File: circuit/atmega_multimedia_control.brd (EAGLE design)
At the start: 98.7 x 81.3 mm, 12 parts, among them IC1 MEGA8-P, Q1 20Mhz

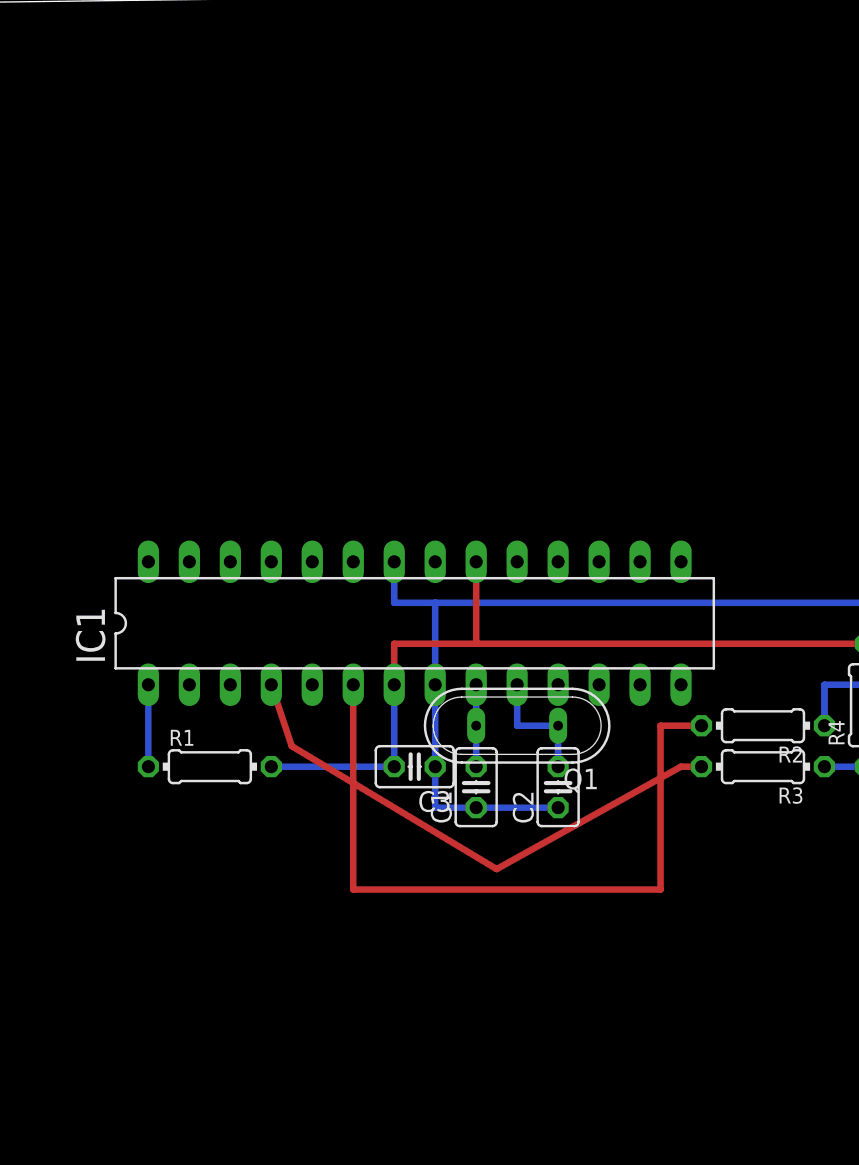
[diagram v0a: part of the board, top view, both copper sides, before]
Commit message: circuit and board done
volume knob is missing from board. some led resistors still need proper
placement, will sort that out during soldering
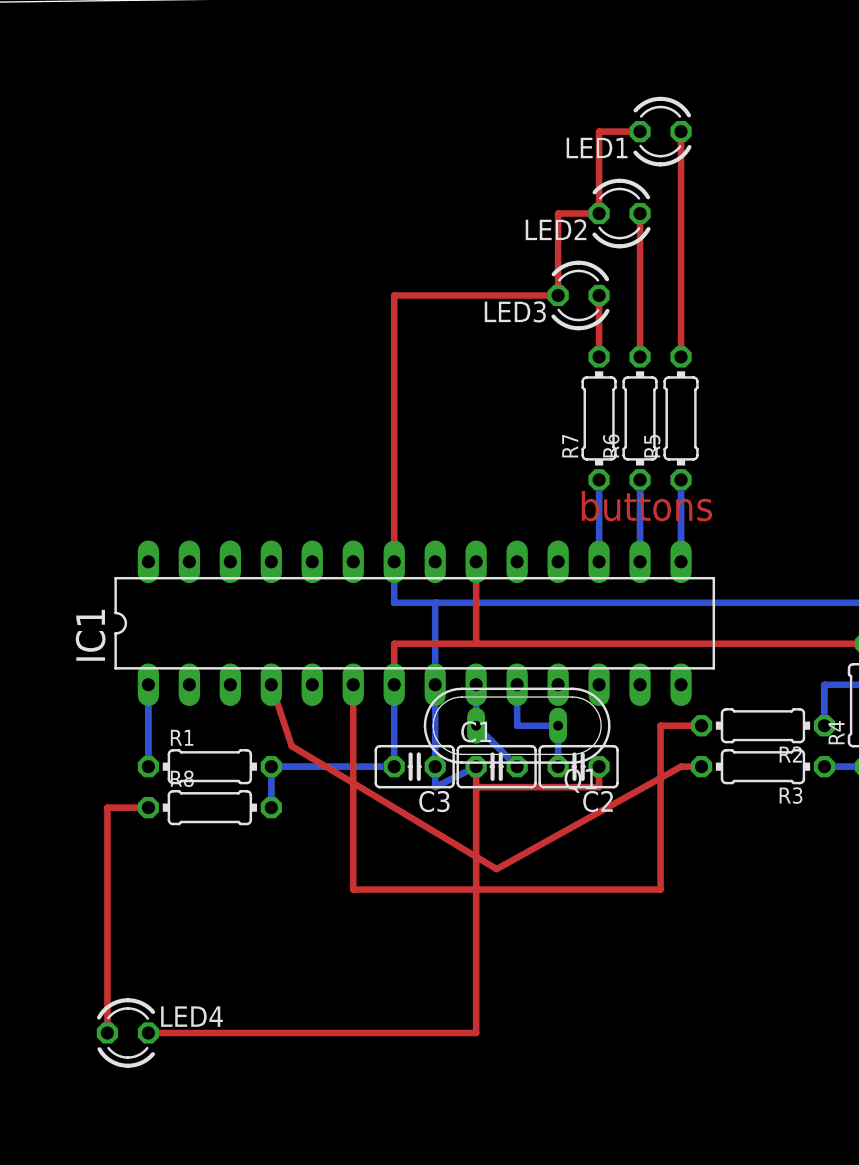
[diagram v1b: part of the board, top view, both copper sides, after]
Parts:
- added LED1, LED2, LED3, LED4: (no value), led:LED3MM
- added R5, R6, R7, R8: 2k2, rcl:0204/7
- X1: value (none) -> USB
- moved C1 1.80 mm to (63.5, 33.0), turned to 0 degrees
- moved C2 1.80 mm to (68.6, 33.0), turned to 180 degrees
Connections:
- removed net +5V: C3.2, IC1.20, IC1.7, R1.2, R4.2, X1.1
- new net N$10: LED1.A, R5.2
- new net N$11: IC1.16, R6.1
- new net N$12: LED2.A, R6.2
- new net N$13: IC1.17, R7.1
- new net N$14: LED3.A, R7.2
- new net N$15: LED4.A, R8.1
- new net N$9: IC1.15, R5.1
- new net VCC: C3.2, IC1.20, IC1.7, R1.2, R4.2, R8.2, X1.1
- net GND: now also LED1.K, LED2.K, LED3.K, LED4.K
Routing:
- net GND: track 70.0 -> 151.6 mm
- net VCC: track 0.00 -> 60.1 mm
- net +5V: track 57.5 -> 0.00 mm
- net N$15: track 0.00 -> 16.5 mm
- net N$10: track 0.00 -> 14.0 mm
- net N$12: track 0.00 -> 8.89 mm
- net N$9: track 0.00 -> 5.08 mm
- net N$13: track 0.00 -> 5.08 mm
- net N$11: track 0.00 -> 5.08 mm
- net N$14: track 0.00 -> 3.81 mm
- net N$2: track 5.08 -> 6.13 mm
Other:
- board text added: "buttons"
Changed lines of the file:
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@@
 <wire x1="98.73" y1="81.27" x2="0" y2="80" width="0" layer="20"/>
 <wire x1="0" y1="80" x2="0" y2="0" width="0" layer="20"/>
+<text x="68.58" y="48.26" size="1.778" layer="1">buttons</text>
 </plain>
 <attributes>
@@
 <attribute name="OC_FARNELL" value="unknown" x="90.17" y="16.51" size="1.778" layer="27" display="off"/>
 </element>
-<element name="C1" library="rcl" package="C025-025X050" value="22p" x="62.23" y="31.75" rot="R90"/>
+<element name="C1" library="rcl" package="C025-025X050" value="22p" x="63.5" y="33.02"/>
 <element name="R1" library="rcl" package="0204/7" value="100k" x="45.72" y="33.02"/>
-<element name="C2" library="rcl" package="C025-025X050" value="22p" x="67.31" y="31.75" rot="R90"/>
-<element name="X1" library="con-berg" package="PN61729" value="" x="99.06" y="39.37" rot="R90">
+<element name="C2" library="rcl" package="C025-025X050" value="22p" x="68.58" y="33.02" rot="R180"/>
+<element name="X1" library="con-berg" package="PN61729" value="USB" x="99.06" y="39.37" rot="R90">
 <attribute name="OC_NEWARK" value="unknown" x="110.49" y="59.69" size="1.778" layer="27" rot="R90" display="off"/>
 <attribute name="MPN" value="" x="110.49" y="59.69" size="1.778" layer="27" rot="R90" display="off"/>
@@
 <element name="R4" library="rcl" package="0204/7" value="2k2" x="86.36" y="36.83" rot="R90"/>
 <element name="C3" library="rcl" package="C025-025X050" value="100n" x="58.42" y="33.02" rot="R180"/>
+<element name="LED1" library="led" package="LED3MM" value="" x="73.66" y="72.39" rot="R180"/>
+<element name="LED2" library="led" package="LED3MM" value="" x="71.12" y="67.31" rot="R180"/>
+<element name="LED3" library="led" package="LED3MM" value="" x="68.58" y="62.23" rot="R180"/>
+<element name="R5" library="rcl" package="0204/7" value="2k2" x="74.93" y="54.61" rot="R90"/>
+<element name="R6" library="rcl" package="0204/7" value="2k2" x="72.39" y="54.61" rot="R90"/>
+<element name="R7" library="rcl" package="0204/7" value="2k2" x="69.85" y="54.61" rot="R90"/>
+<element name="LED4" library="led" package="LED3MM" value="" x="40.64" y="16.51"/>
+<element name="R8" library="rcl" package="0204/7" value="2k2" x="45.72" y="30.48"/>
 </elements>
 <signals>
-<signal name="+5V">
-<contactref element="R1" pad="2"/>
-<contactref element="IC1" pad="20"/>
-<contactref element="X1" pad="1"/>
-<contactref element="R4" pad="2"/>
-<contactref element="C3" pad="2"/>
-<wire x1="57.15" y1="40.64" x2="62.23" y2="40.64" width="0.4064" layer="1"/>
-<wire x1="62.23" y1="40.64" x2="62.23" y2="45.72" width="0.4064" layer="1"/>
-<wire x1="94.35" y1="40.62" x2="86.36" y2="40.62" width="0.4064" layer="16"/>
-<wire x1="86.36" y1="40.62" x2="86.36" y2="40.64" width="0.4064" layer="16"/>
-<contactref element="IC1" pad="7"/>
-<wire x1="49.53" y1="33.02" x2="57.15" y2="33.02" width="0.4064" layer="16"/>
-<wire x1="57.15" y1="33.02" x2="57.15" y2="38.1" width="0.4064" layer="16"/>
-<wire x1="57.15" y1="38.1" x2="57.15" y2="40.64" width="0.4064" layer="1"/>
-<wire x1="62.23" y1="40.64" x2="86.36" y2="40.64" width="0.4064" layer="1"/>
-</signal>
 <signal name="N$1">
 <contactref element="R1" pad="1"/>
@@
 <contactref element="C1" pad="1"/>
 <contactref element="C2" pad="1"/>
-<wire x1="59.69" y1="33.02" x2="59.69" y2="30.48" width="0.4064" layer="16"/>
-<wire x1="59.69" y1="30.48" x2="62.23" y2="30.48" width="0.4064" layer="16"/>
-<wire x1="62.23" y1="30.48" x2="67.31" y2="30.48" width="0.4064" layer="16"/>
+<wire x1="59.69" y1="33.02" x2="59.69" y2="31.75" width="0.4064" layer="16"/>
+<wire x1="59.69" y1="31.75" x2="62.23" y2="33.02" width="0.4064" layer="16"/>
+<contactref element="LED1" pad="K"/>
+<contactref element="LED2" pad="K"/>
+<contactref element="LED3" pad="K"/>
+<contactref element="LED4" pad="K"/>
+<wire x1="67.31" y1="62.23" x2="57.15" y2="62.23" width="0.4064" layer="1"/>
+<wire x1="57.15" y1="62.23" x2="57.15" y2="45.72" width="0.4064" layer="1"/>
+<wire x1="67.31" y1="62.23" x2="67.31" y2="67.31" width="0.4064" layer="1"/>
+<wire x1="67.31" y1="67.31" x2="69.85" y2="67.31" width="0.4064" layer="1"/>
+<wire x1="69.85" y1="67.31" x2="69.85" y2="72.39" width="0.4064" layer="1"/>
+<wire x1="69.85" y1="72.39" x2="72.39" y2="72.39" width="0.4064" layer="1"/>
+<wire x1="41.91" y1="16.51" x2="62.23" y2="16.51" width="0.4064" layer="1"/>
+<wire x1="62.23" y1="16.51" x2="62.23" y2="31.75" width="0.4064" layer="1"/>
+<wire x1="62.23" y1="33.02" x2="62.23" y2="31.75" width="0.4064" layer="1"/>
+<wire x1="62.23" y1="31.75" x2="69.85" y2="31.75" width="0.4064" layer="1"/>
+<wire x1="69.85" y1="31.75" x2="69.85" y2="33.02" width="0.4064" layer="1"/>
 </signal>
 <signal name="N$6">
@@
 <contactref element="IC1" pad="9"/>
 <wire x1="62.23" y1="38.1" x2="62.23" y2="35.56" width="0.4064" layer="16"/>
-<wire x1="62.23" y1="35.56" x2="62.23" y2="33.02" width="0.4064" layer="16"/>
+<wire x1="62.23" y1="35.56" x2="64.77" y2="33.02" width="0.4064" layer="16"/>
 </signal>
 <signal name="N$3">
@@
 <wire x1="64.77" y1="35.56" x2="64.77" y2="38.1" width="0.4064" layer="16"/>
 </signal>
+<signal name="N$9">
+<contactref element="IC1" pad="15"/>
+<contactref element="R5" pad="1"/>
+<wire x1="74.93" y1="50.8" x2="74.93" y2="45.72" width="0.4064" layer="16"/>
+</signal>
+<signal name="N$10">
+<contactref element="R5" pad="2"/>
+<contactref element="LED1" pad="A"/>
+<wire x1="74.93" y1="58.42" x2="74.93" y2="72.39" width="0.4064" layer="1"/>
+</signal>
+<signal name="N$11">
+<contactref element="IC1" pad="16"/>
+<contactref element="R6" pad="1"/>
+<wire x1="72.39" y1="50.8" x2="72.39" y2="45.72" width="0.4064" layer="16"/>
+</signal>
+<signal name="N$12">
+<contactref element="R6" pad="2"/>
+<contactref element="LED2" pad="A"/>
+<wire x1="72.39" y1="58.42" x2="72.39" y2="67.31" width="0.4064" layer="1"/>
+</signal>
+<signal name="N$13">
+<contactref element="IC1" pad="17"/>
+<contactref element="R7" pad="1"/>
+<wire x1="69.85" y1="50.8" x2="69.85" y2="45.72" width="0.4064" layer="16"/>
+</signal>
+<signal name="N$14">
+<contactref element="R7" pad="2"/>
+<contactref element="LED3" pad="A"/>
+<wire x1="69.85" y1="58.42" x2="69.85" y2="62.23" width="0.4064" layer="1"/>
+</signal>
+<signal name="N$15">
+<contactref element="LED4" pad="A"/>
+<contactref element="R8" pad="1"/>
+<wire x1="41.91" y1="30.48" x2="39.37" y2="30.48" width="0.4064" layer="1"/>
+<wire x1="39.37" y1="30.48" x2="39.37" y2="16.51" width="0.4064" layer="1"/>
+</signal>
+<signal name="VCC">
+<contactref element="R1" pad="2"/>
+<contactref element="IC1" pad="20"/>
+<contactref element="X1" pad="1"/>
+<contactref element="R4" pad="2"/>
+<contactref element="C3" pad="2"/>
+<contactref element="IC1" pad="7"/>
+<contactref element="R8" pad="2"/>
+<wire x1="57.15" y1="40.64" x2="62.23" y2="40.64" width="0.4064" layer="1"/>
+<wire x1="62.23" y1="40.64" x2="62.23" y2="45.72" width="0.4064" layer="1"/>
+<wire x1="94.35" y1="40.62" x2="86.36" y2="40.62" width="0.4064" layer="16"/>
+<wire x1="86.36" y1="40.62" x2="86.36" y2="40.64" width="0.4064" layer="16"/>
+<wire x1="49.53" y1="33.02" x2="57.15" y2="33.02" width="0.4064" layer="16"/>
+<wire x1="57.15" y1="33.02" x2="57.15" y2="38.1" width="0.4064" layer="16"/>
+<wire x1="57.15" y1="38.1" x2="57.15" y2="40.64" width="0.4064" layer="1"/>
+<wire x1="62.23" y1="40.64" x2="86.36" y2="40.64" width="0.4064" layer="1"/>
+<wire x1="49.53" y1="33.02" x2="49.53" y2="30.48" width="0.4064" layer="16"/>
+</signal>
 </signals>

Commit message: fixed schematic
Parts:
- moved R2 2.54 mm to (80.0, 33.0)
- moved R3 2.54 mm to (80.0, 35.6)
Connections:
- removed net N$5 (its old number): D2.C, R3.1, R4.1, X1.3
- removed net N$6: D1.C, R2.1, X1.2
- new net N$16: D1.C, R2.1, R4.1, X1.2
- new net N$4: D2.C, R3.1, X1.3
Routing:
- net N$16: track 0.00 -> 18.2 mm
- net N$5 (its old number): track 18.0 -> 0.00 mm
- net N$4: track 0.00 -> 15.4 mm
- net N$7: track 33.2 -> 47.0 mm
- net N$6: track 13.1 -> 0.00 mm
- net N$5: track 44.5 -> 34.3 mm
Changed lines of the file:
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@@
 <element name="D1" library="diode" package="DO34Z7" value="3v6" x="91.44" y="41.91" rot="R90"/>
 <element name="D2" library="diode" package="DO34Z7" value="3v6" x="88.9" y="39.37" rot="R90"/>
-<element name="R2" library="rcl" package="0204/7" value="68" x="80.01" y="35.56" rot="R180"/>
-<element name="R3" library="rcl" package="0204/7" value="68" x="80.01" y="33.02" rot="R180"/>
+<element name="R2" library="rcl" package="0204/7" value="68" x="80.01" y="33.02" rot="R180"/>
+<element name="R3" library="rcl" package="0204/7" value="68" x="80.01" y="35.56" rot="R180"/>
 <element name="Q1" library="special" package="QS" value="20Mhz" x="64.77" y="35.56" rot="R180"/>
 <element name="R4" library="rcl" package="0204/7" value="2k2" x="86.36" y="36.83" rot="R90"/>
@@
 <wire x1="62.23" y1="31.75" x2="69.85" y2="31.75" width="0.4064" layer="1"/>
 <wire x1="69.85" y1="31.75" x2="69.85" y2="33.02" width="0.4064" layer="1"/>
-</signal>
-<signal name="N$6">
-<contactref element="X1" pad="2"/>
-<contactref element="R2" pad="1"/>
-<contactref element="D1" pad="C"/>
-<wire x1="91.44" y1="38.1" x2="94.35" y2="38.1" width="0.4064" layer="16"/>
-<wire x1="94.35" y1="38.1" x2="94.35" y2="38.12" width="0.4064" layer="16"/>
-<wire x1="83.82" y1="35.56" x2="83.82" y2="38.1" width="0.4064" layer="16"/>
-<wire x1="83.82" y1="38.1" x2="91.44" y2="38.1" width="0.4064" layer="16"/>
-</signal>
-<signal name="N$4">
-<contactref element="R2" pad="2"/>
-<contactref element="IC1" pad="6"/>
-<wire x1="76.2" y1="35.56" x2="73.66" y2="35.56" width="0.4064" layer="1"/>
-<wire x1="73.66" y1="35.56" x2="73.66" y2="25.4" width="0.4064" layer="1"/>
-<wire x1="73.66" y1="25.4" x2="54.61" y2="25.4" width="0.4064" layer="1"/>
-<wire x1="54.61" y1="25.4" x2="54.61" y2="38.1" width="0.4064" layer="1"/>
-</signal>
-<signal name="N$5">
-<contactref element="R3" pad="1"/>
-<contactref element="X1" pad="3"/>
-<contactref element="R4" pad="1"/>
-<contactref element="D2" pad="C"/>
-<wire x1="96.35" y1="38.12" x2="96.52" y2="38.12" width="0.4064" layer="16"/>
-<wire x1="96.52" y1="38.12" x2="96.52" y2="35.56" width="0.4064" layer="16"/>
-<wire x1="96.52" y1="35.56" x2="88.9" y2="35.56" width="0.4064" layer="16"/>
-<wire x1="88.9" y1="35.56" x2="88.9" y2="33.02" width="0.4064" layer="16"/>
-<wire x1="88.9" y1="33.02" x2="86.36" y2="33.02" width="0.4064" layer="16"/>
-<wire x1="83.82" y1="33.02" x2="86.36" y2="33.02" width="0.4064" layer="16"/>
-</signal>
-<signal name="N$7">
-<contactref element="R3" pad="2"/>
-<contactref element="IC1" pad="4"/>
-<wire x1="49.53" y1="38.1" x2="50.8" y2="34.29" width="0.4064" layer="1"/>
-<wire x1="50.8" y1="34.29" x2="63.5" y2="26.67" width="0.4064" layer="1"/>
-<wire x1="63.5" y1="26.67" x2="74.93" y2="33.02" width="0.4064" layer="1"/>
-<wire x1="74.93" y1="33.02" x2="76.2" y2="33.02" width="0.4064" layer="1"/>
 </signal>
 <signal name="N$8">
@@
 <wire x1="49.53" y1="33.02" x2="49.53" y2="30.48" width="0.4064" layer="16"/>
 </signal>
+<signal name="N$4">
+<contactref element="X1" pad="3"/>
+<contactref element="D2" pad="C"/>
+<wire x1="96.35" y1="38.12" x2="96.52" y2="38.12" width="0.4064" layer="16"/>
+<wire x1="96.52" y1="38.12" x2="96.52" y2="35.56" width="0.4064" layer="16"/>
+<wire x1="96.52" y1="35.56" x2="88.9" y2="35.56" width="0.4064" layer="16"/>
+<contactref element="R3" pad="1"/>
+<wire x1="83.82" y1="35.56" x2="88.9" y2="35.56" width="0.4064" layer="1"/>
+</signal>
+<signal name="N$5">
+<contactref element="R2" pad="2"/>
+<contactref element="IC1" pad="6"/>
+<wire x1="76.2" y1="33.02" x2="76.2" y2="29.21" width="0.4064" layer="1"/>
+<wire x1="76.2" y1="29.21" x2="54.61" y2="29.21" width="0.4064" layer="1"/>
+<wire x1="54.61" y1="29.21" x2="54.61" y2="38.1" width="0.4064" layer="1"/>
+</signal>
+<signal name="N$7">
+<contactref element="IC1" pad="4"/>
+<contactref element="R3" pad="2"/>
+<wire x1="76.2" y1="35.56" x2="73.66" y2="35.56" width="0.4064" layer="1"/>
+<wire x1="73.66" y1="35.56" x2="73.66" y2="26.67" width="0.4064" layer="1"/>
+<wire x1="73.66" y1="26.67" x2="52.07" y2="26.67" width="0.4064" layer="1"/>
+<wire x1="52.07" y1="26.67" x2="52.07" y2="35.56" width="0.4064" layer="1"/>
+<wire x1="52.07" y1="35.56" x2="49.53" y2="35.56" width="0.4064" layer="1"/>
+<wire x1="49.53" y1="35.56" x2="49.53" y2="38.1" width="0.4064" layer="1"/>
+</signal>
+<signal name="N$16">
+<contactref element="X1" pad="2"/>
+<contactref element="D1" pad="C"/>
+<wire x1="91.44" y1="38.1" x2="94.35" y2="38.1" width="0.4064" layer="16"/>
+<wire x1="94.35" y1="38.1" x2="94.35" y2="38.12" width="0.4064" layer="16"/>
+<wire x1="83.82" y1="38.1" x2="91.44" y2="38.1" width="0.4064" layer="16"/>
+<contactref element="R4" pad="1"/>
+<contactref element="R2" pad="1"/>
+<wire x1="83.82" y1="33.02" x2="83.82" y2="38.1" width="0.4064" layer="16"/>
+<wire x1="83.82" y1="33.02" x2="86.36" y2="33.02" width="0.4064" layer="16"/>
+</signal>
 </signals>
